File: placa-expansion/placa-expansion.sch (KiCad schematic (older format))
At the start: 1 part

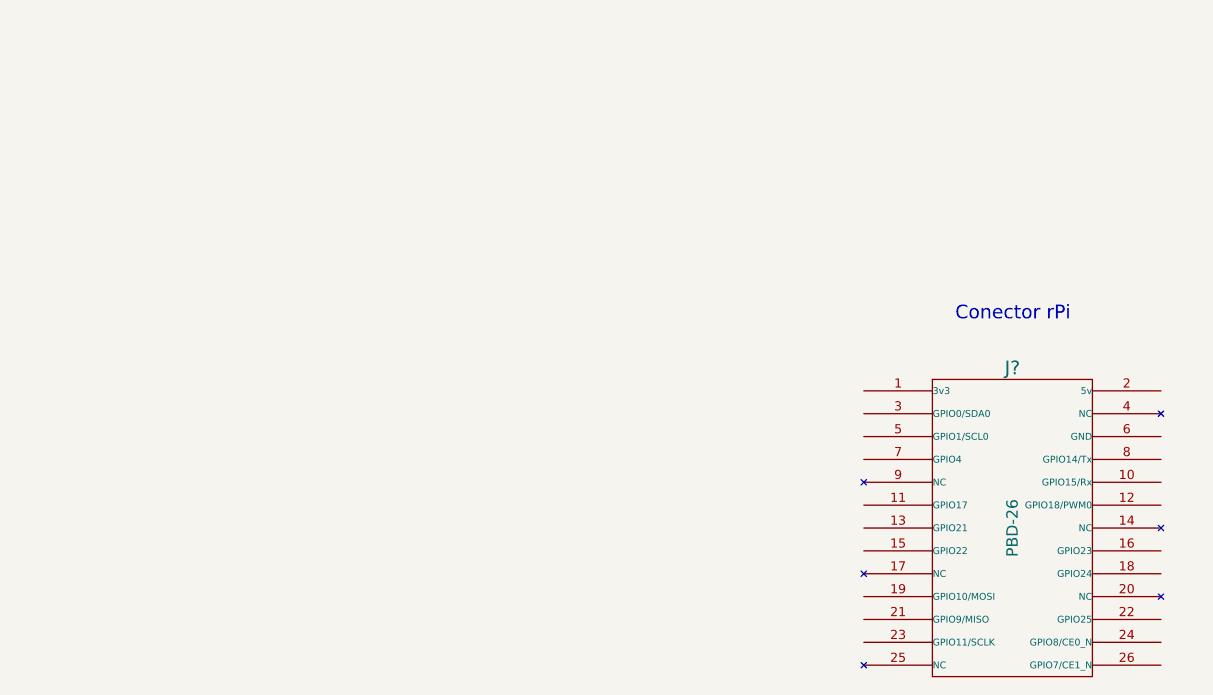
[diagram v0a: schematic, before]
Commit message: Agregamos los conectores al esquematico.
Falta poner la interfaz en los pines Tx y Rx entre el 3pi y el rPi.
Falta tambien agregar el regulador para la rPi.
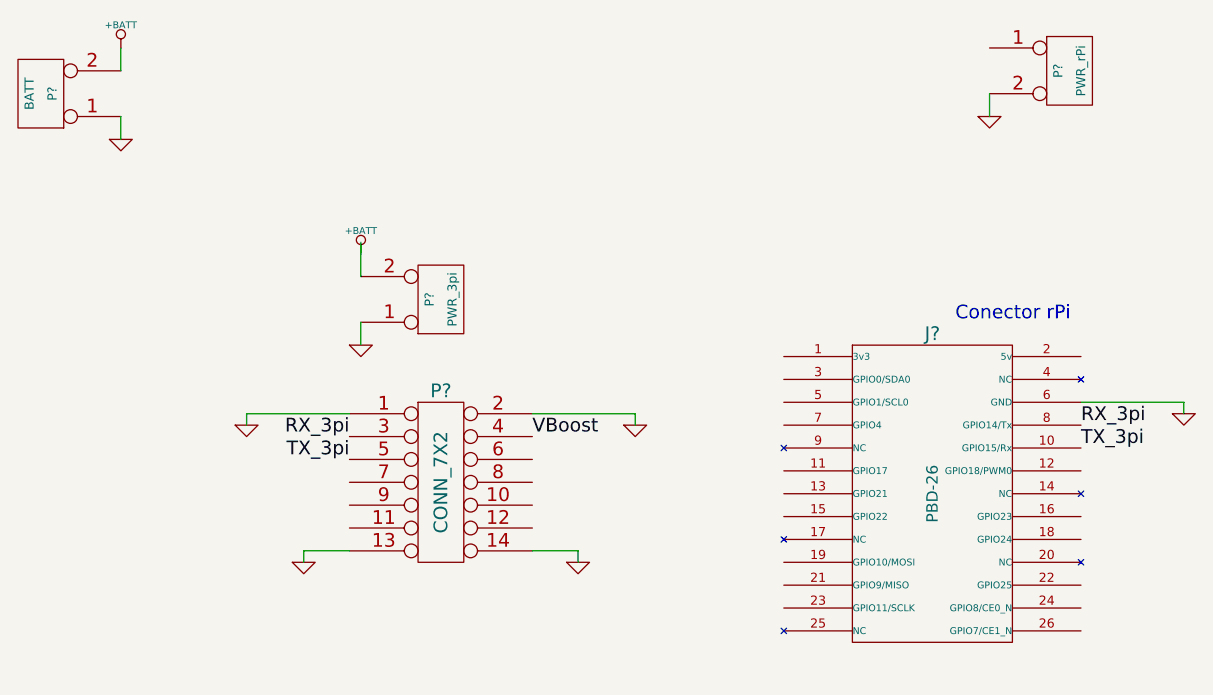
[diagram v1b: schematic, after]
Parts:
- added P?: CONN_7X2, ~, symbol CONN_7X2
- added P?: PWR_rPi, ~, symbol CONN_2
- added P?: BATT, ~, symbol CONN_2
- added P?: PWR_3pi, ~, symbol CONN_2
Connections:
- net labels added: +BATT, GND, RX_3pi, TX_3pi, VBoost
- wire segments 0 -> 15
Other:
- moved on the sheet: J?
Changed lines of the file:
@@
-EESchema Schematic File Version 2  date dom 21 abr 2013 10:59:05 ART
+EESchema Schematic File Version 2  date vie 26 abr 2013 22:01:33 ART
 LIBS:power
 LIBS:device
@@
 LIBS:valves
 LIBS:Conn-raspberry
-EELAYER 43  0
+EELAYER 27 0
 EELAYER END
-$Descr A4 11700 8267
+$Descr A4 11693 8268
 encoding utf-8
 Sheet 1 1
 Title "Expansión para el 3pi - Raspberry Pi"
-Date "21 apr 2013"
+Date "27 apr 2013"
 Rev "0.1"
 Comp "Club de Robótica FIUBA"
@@
 L PBD-26 J?
 U 1 1 5173EFB3
-P 8700 3700
-F 0 "J?" H 8700 4400 60  0000 C CNN
-F 1 "PBD-26" V 8700 3700 50  0000 C CNN
-	1    8700 3700
-	1    0    0    -1
-$EndComp
+P 8350 3550
+F 0 "J?" H 8350 4250 60  0000 C CNN
+F 1 "PBD-26" V 8350 3550 50  0000 C CNN
+F 2 "" H 8350 3550 60  0001 C CNN
+F 3 "" H 8350 3550 60  0001 C CNN
+	1    8350 3550
+	1    0    0    -1
+$EndComp
+$Comp
+L CONN_7X2 P?
+U 1 1 517B09E6
+P 6200 3500
+F 0 "P?" H 6200 3900 60  0000 C CNN
+F 1 "CONN_7X2" V 6200 3500 60  0000 C CNN
+F 2 "~" H 6200 3500 60  0000 C CNN
+F 3 "~" H 6200 3500 60  0000 C CNN
+	1    6200 3500
+	1    0    0    -1
+$EndComp
+Text Label 5800 3400 2    60   ~ 0
+TX_3pi
+Text Label 5800 3300 2    60   ~ 0
+RX_3pi
+Text Label 9000 3250 0    60   ~ 0
+RX_3pi
+Text Label 9000 3350 0    60   ~ 0
+TX_3pi
+$Comp
+L CONN_2 P?
+U 1 1 517B1B1A
+P 8950 1700
+F 0 "P?" V 8900 1700 40  0000 C CNN
+F 1 "PWR_rPi" V 9000 1700 40  0000 C CNN
+F 2 "~" H 8950 1700 60  0000 C CNN
+F 3 "~" H 8950 1700 60  0000 C CNN
+	1    8950 1700
+	1    0    0    -1
+$EndComp
+$Comp
+L CONN_2 P?
+U 1 1 517B1B29
+P 4450 1800
+F 0 "P?" V 4400 1800 40  0000 C CNN
+F 1 "BATT" V 4500 1800 40  0000 C CNN
+F 2 "~" H 4450 1800 60  0000 C CNN
+F 3 "~" H 4450 1800 60  0000 C CNN
+	1    4450 1800
+	-1   0    0    1
+$EndComp
+$Comp
+L CONN_2 P?
+U 1 1 517B1B4B
+P 6200 2700
+F 0 "P?" V 6150 2700 40  0000 C CNN
+F 1 "PWR_3pi" V 6250 2700 40  0000 C CNN
+F 2 "~" H 6200 2700 60  0000 C CNN
+F 3 "~" H 6200 2700 60  0000 C CNN
+	1    6200 2700
+	1    0    0    1
+$EndComp
+$Comp
+L GND #PWR?
+U 1 1 517B1C23
+P 4800 2000
+F 0 "#PWR?" H 4800 2000 30  0001 C CNN
+F 1 "GND" H 4800 1930 30  0001 C CNN
+F 2 "" H 4800 2000 60  0000 C CNN
+F 3 "" H 4800 2000 60  0000 C CNN
+	1    4800 2000
+	1    0    0    -1
+$EndComp
+$Comp
+L GND #PWR?
+U 1 1 517B1C32
+P 5850 2900
+F 0 "#PWR?" H 5850 2900 30  0001 C CNN
+F 1 "GND" H 5850 2830 30  0001 C CNN
+F 2 "" H 5850 2900 60  0000 C CNN
+F 3 "" H 5850 2900 60  0000 C CNN
+	1    5850 2900
+	1    0    0    -1
+$EndComp
+$Comp
+L GND #PWR?
+U 1 1 517B1C41
+P 5350 3250
+F 0 "#PWR?" H 5350 3250 30  0001 C CNN
+F 1 "GND" H 5350 3180 30  0001 C CNN
+F 2 "" H 5350 3250 60  0000 C CNN
+F 3 "" H 5350 3250 60  0000 C CNN
+	1    5350 3250
+	1    0    0    -1
+$EndComp
+$Comp
+L GND #PWR?
+U 1 1 517B1C58
+P 7050 3250
+F 0 "#PWR?" H 7050 3250 30  0001 C CNN
+F 1 "GND" H 7050 3180 30  0001 C CNN
+F 2 "" H 7050 3250 60  0000 C CNN
+F 3 "" H 7050 3250 60  0000 C CNN
+	1    7050 3250
+	1    0    0    -1
+$EndComp
+$Comp
+L GND #PWR?
+U 1 1 517B1C67
+P 5600 3850
+F 0 "#PWR?" H 5600 3850 30  0001 C CNN
+F 1 "GND" H 5600 3780 30  0001 C CNN
+F 2 "" H 5600 3850 60  0000 C CNN
+F 3 "" H 5600 3850 60  0000 C CNN
+	1    5600 3850
+	1    0    0    -1
+$EndComp
+$Comp
+L GND #PWR?
+U 1 1 517B1C76
+P 6800 3850
+F 0 "#PWR?" H 6800 3850 30  0001 C CNN
+F 1 "GND" H 6800 3780 30  0001 C CNN
+F 2 "" H 6800 3850 60  0000 C CNN
+F 3 "" H 6800 3850 60  0000 C CNN
+	1    6800 3850
+	1    0    0    -1
+$EndComp
+$Comp
+L GND #PWR?
+U 1 1 517B1C85
+P 9450 3200
+F 0 "#PWR?" H 9450 3200 30  0001 C CNN
+F 1 "GND" H 9450 3130 30  0001 C CNN
+F 2 "" H 9450 3200 60  0000 C CNN
+F 3 "" H 9450 3200 60  0000 C CNN
+	1    9450 3200
+	1    0    0    -1
+$EndComp
+Wire Wire Line
+	6600 3200 7050 3200
+Wire Wire Line
+	7050 3200 7050 3250
+Wire Wire Line
+	6600 3800 6800 3800
+Wire Wire Line
+	6800 3800 6800 3850
+Wire Wire Line
+	5800 3800 5600 3800
+Wire Wire Line
+	5600 3800 5600 3850
+Wire Wire Line
+	5800 3200 5350 3200
+Wire Wire Line
+	5350 3200 5350 3250
+Wire Wire Line
+	5850 2900 5850 2800
+Wire Wire Line
+	9000 3150 9450 3150
+Wire Wire Line
+	9450 3150 9450 3200
+Wire Wire Line
+	4800 1900 4800 2000
+$Comp
+L GND #PWR?
+U 1 1 517B1CE1
+P 8600 1900
+F 0 "#PWR?" H 8600 1900 30  0001 C CNN
+F 1 "GND" H 8600 1830 30  0001 C CNN
+F 2 "" H 8600 1900 60  0000 C CNN
+F 3 "" H 8600 1900 60  0000 C CNN
+	1    8600 1900
+	1    0    0    -1
+$EndComp
+Wire Wire Line
+	8600 1800 8600 1900
+$Comp
+L +BATT #PWR?
+U 1 1 517B1D0A
+P 4800 1600
+F 0 "#PWR?" H 4800 1550 20  0001 C CNN
+F 1 "+BATT" H 4800 1700 30  0000 C CNN
+F 2 "" H 4800 1600 60  0000 C CNN
+F 3 "" H 4800 1600 60  0000 C CNN
+	1    4800 1600
+	1    0    0    -1
+$EndComp
+$Comp
+L +BATT #PWR?
+U 1 1 517B1D19
+P 5850 2500
+F 0 "#PWR?" H 5850 2450 20  0001 C CNN
+F 1 "+BATT" H 5850 2600 30  0000 C CNN
+F 2 "" H 5850 2500 60  0000 C CNN
+F 3 "" H 5850 2500 60  0000 C CNN
+	1    5850 2500
+	1    0    0    -1
+$EndComp
+Wire Wire Line
+	5850 2450 5850 2600
+Wire Wire Line
+	4800 1600 4800 1700
+Text Label 6600 3300 0    60   ~ 0
+VBoost
 $EndSCHEMATC

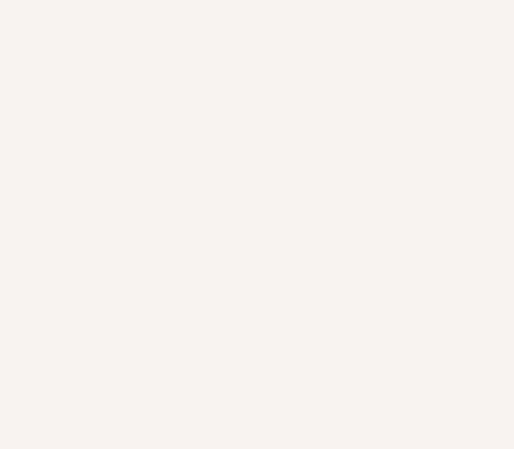
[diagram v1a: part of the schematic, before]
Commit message: El driver que utilizaremos para interfacear el rPi con el 3pi es el TXB0108
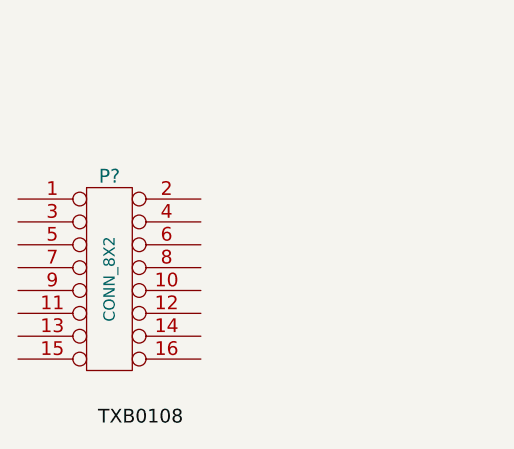
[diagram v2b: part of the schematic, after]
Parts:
- added P?: CONN_8X2, ~, symbol CONN_8X2
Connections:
- net labels added: TXB0108
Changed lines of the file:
@@
-EESchema Schematic File Version 2  date vie 26 abr 2013 22:01:33 ART
+EESchema Schematic File Version 2  date vie 26 abr 2013 22:06:17 ART
 LIBS:power
 LIBS:device
@@
 LIBS:valves
 LIBS:Conn-raspberry
+LIBS:placa-expansion-cache
 EELAYER 27 0
 EELAYER END
@@
 Text Label 6600 3300 0    60   ~ 0
 VBoost
+$Comp
+L CONN_8X2 P?
+U 1 1 517B24BF
+P 1650 4000
+F 0 "P?" H 1650 4450 60  0000 C CNN
+F 1 "CONN_8X2" V 1650 4000 50  0000 C CNN
+F 2 "~" H 1650 4000 60  0000 C CNN
+F 3 "~" H 1650 4000 60  0000 C CNN
+	1    1650 4000
+	1    0    0    -1
+$EndComp
+Text Label 1600 4650 0    60   ~ 0
+TXB0108
 $EndSCHEMATC

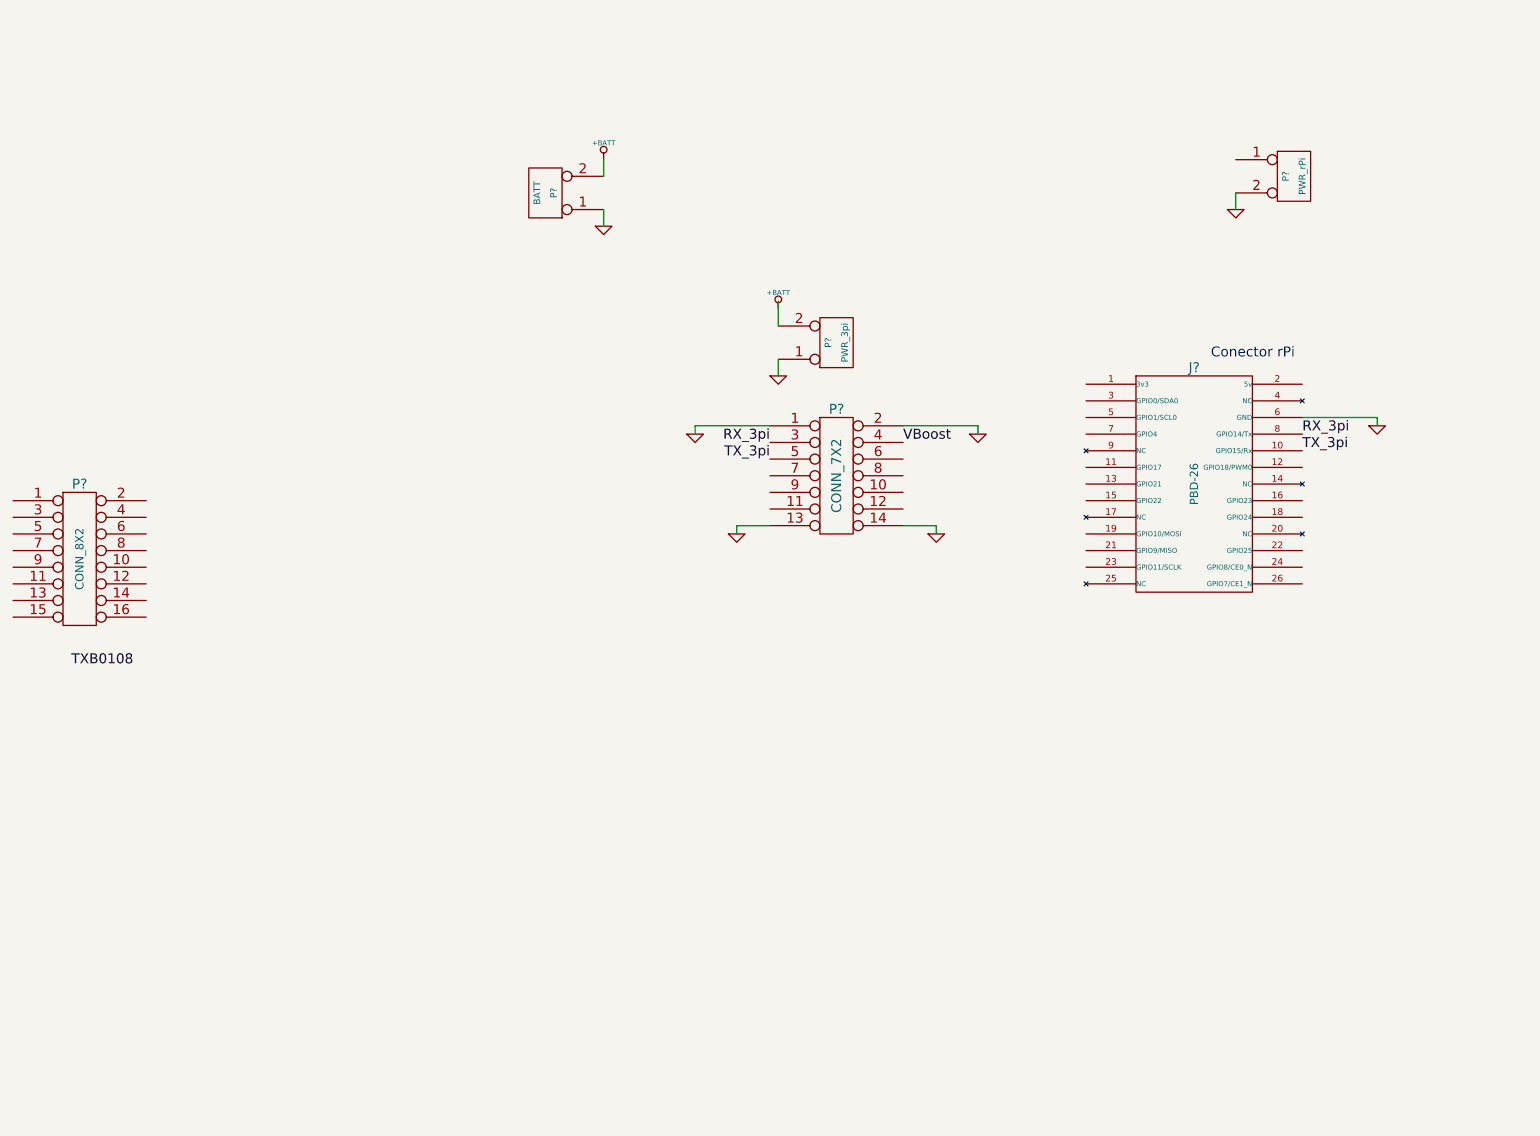
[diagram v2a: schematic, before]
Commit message: Se trabajo sobre el esquemático
Se agrego el integrado buffer y el regulador de 5V para la rPi
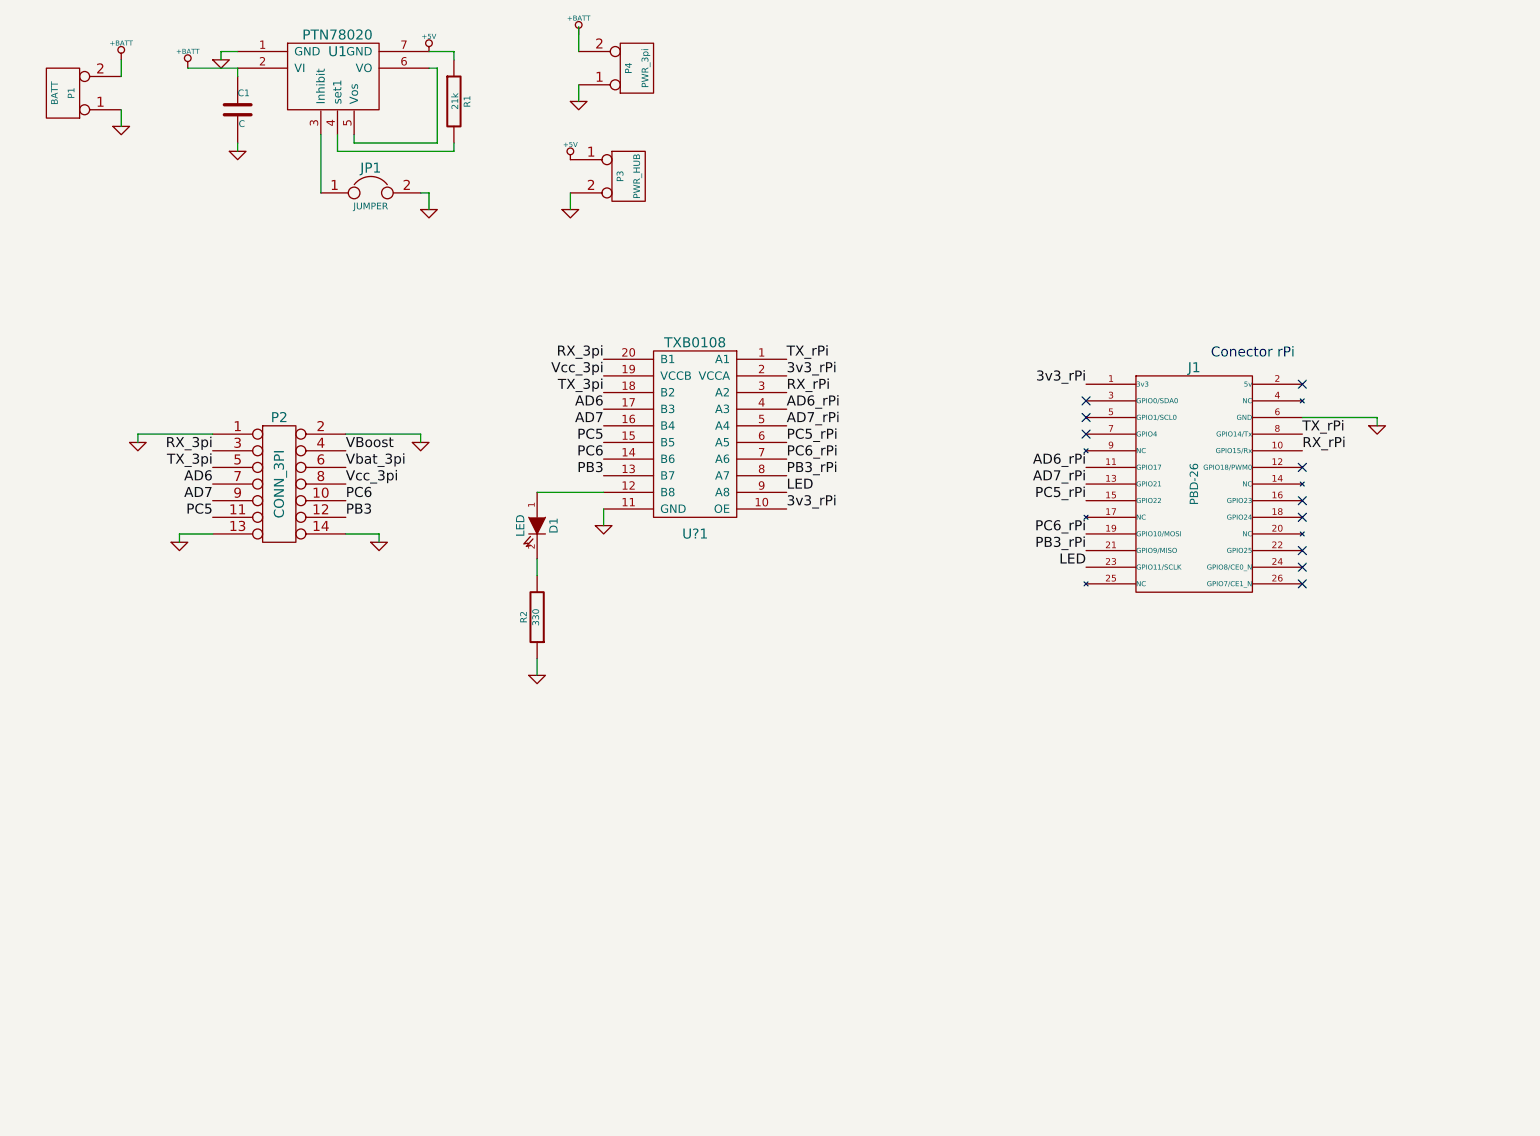
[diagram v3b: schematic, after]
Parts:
- removed P?: CONN_8X2, ~, symbol CONN_8X2
- added C1: C, ~, symbol C
- added D1: LED, ~, symbol LED
- added JP1: JUMPER, ~, symbol JUMPER
- added R1: 21k, ~, symbol R
- added R2: 330, ~, symbol R
- added U1: PTN78020, ~, symbol PTN78020
- added U?1: TXB0108, ~, symbol TXB0108
- P2: renamed from P?; value CONN_7X2 -> CONN_3PI
- P3: renamed from P?; value PWR_rPi -> PWR_HUB
- gave numbers to parts that had none: 3
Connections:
- net labels added: +5V, 3v3_rPi, AD6, AD6_rPi, AD7, AD7_rPi, LED, PB3, PB3_rPi, PC5, PC5_rPi, PC6, PC6_rPi, RX_rPi, TX_rPi, Vbat_3pi, Vcc_3pi
- net labels removed: TXB0108
- wire segments 15 -> 36
- no-connect marks 0 -> 10
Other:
- moved on the sheet: P1, P2, P3, P4
